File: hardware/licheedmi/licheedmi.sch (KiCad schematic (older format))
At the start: 64 parts, among them J1 Conn_01x09, J2 HDMI_A_PCB, J3 LicheePiNano_LCD, J4 HDMI_A, U1 TDA19988, U2 LicheeNano, U3 TS3DV20812, U4 SC6206B

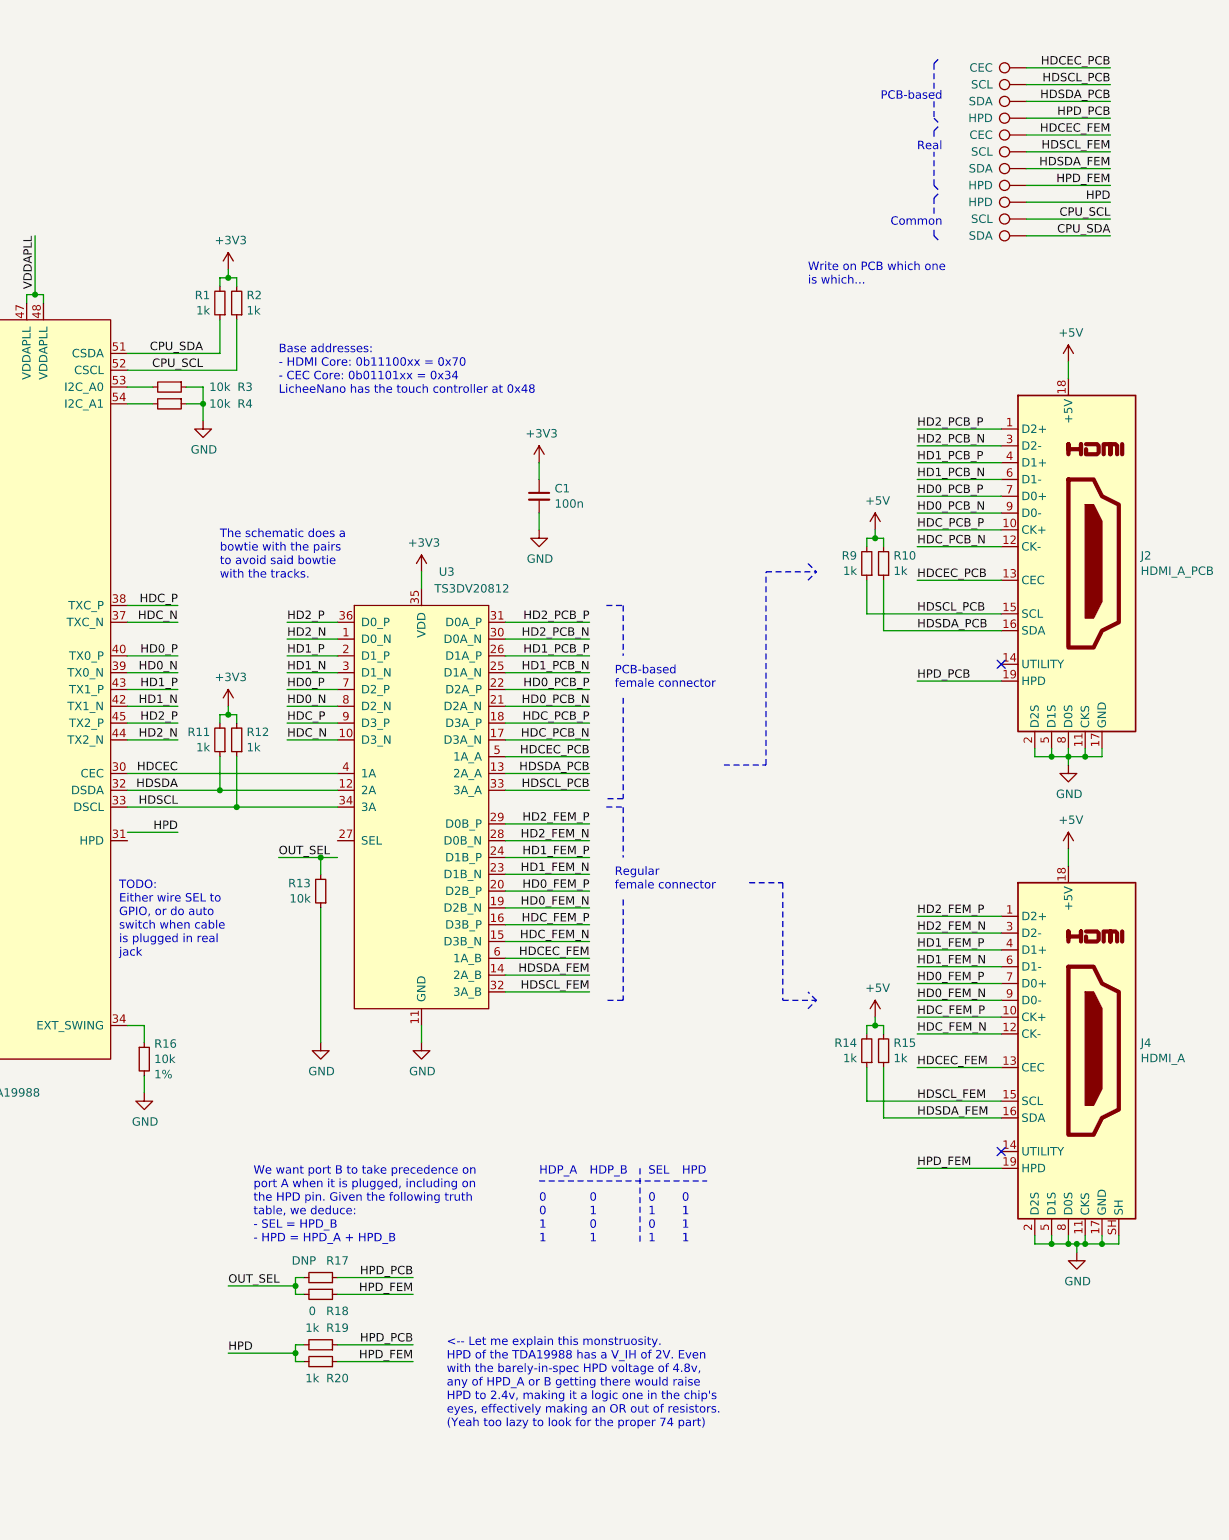
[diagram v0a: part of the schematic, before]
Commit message: sch: Draw wires rather than labels where wiring is straightforward
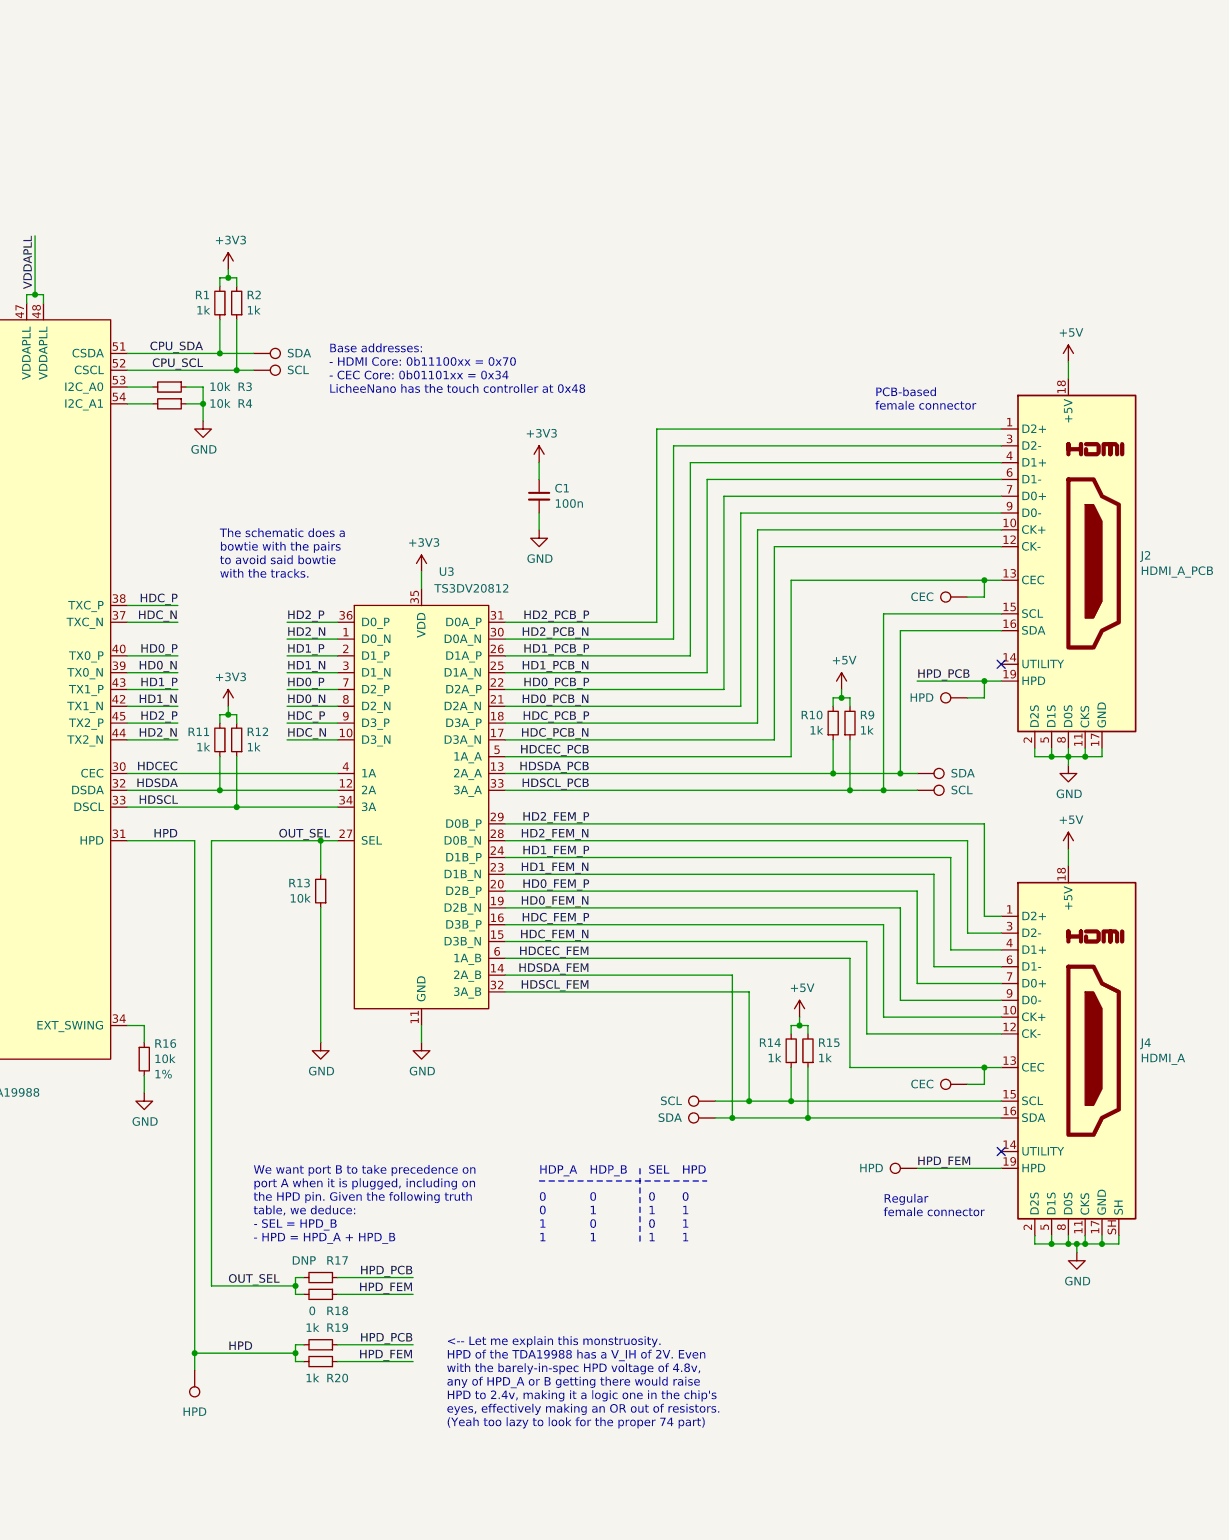
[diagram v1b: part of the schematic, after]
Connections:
- net HPD: now also U1.31 (HPD)
- net OUT_SEL: now also U3.27 (SEL)
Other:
- note removed: "Common"
- note removed: "PCB-based"
- note removed: "Real"
- note removed: "TODO:\nEither wire SEL to\nGPIO, or do auto\nswitch when cable\nis plugged in real\njack"
- note removed: "Write on PCB which one\nis which..."
- moved on the sheet: R10, R14, R15, R9

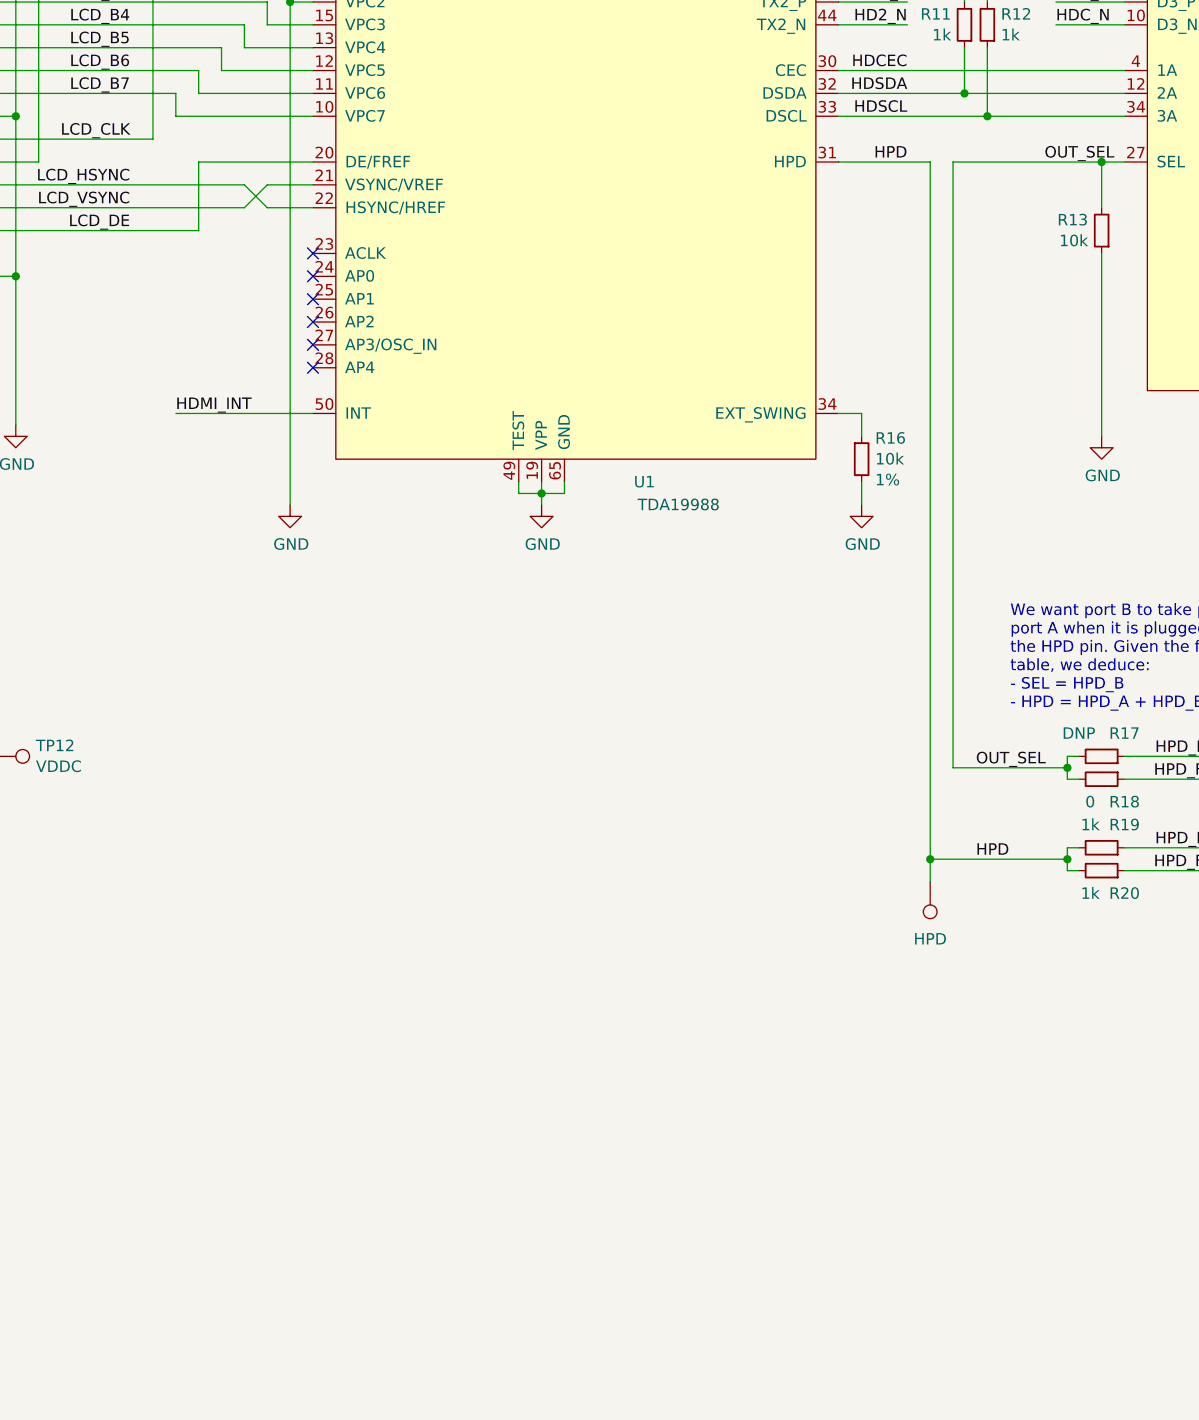
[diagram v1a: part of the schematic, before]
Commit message: *: Add USB-UART chip (CH340C)
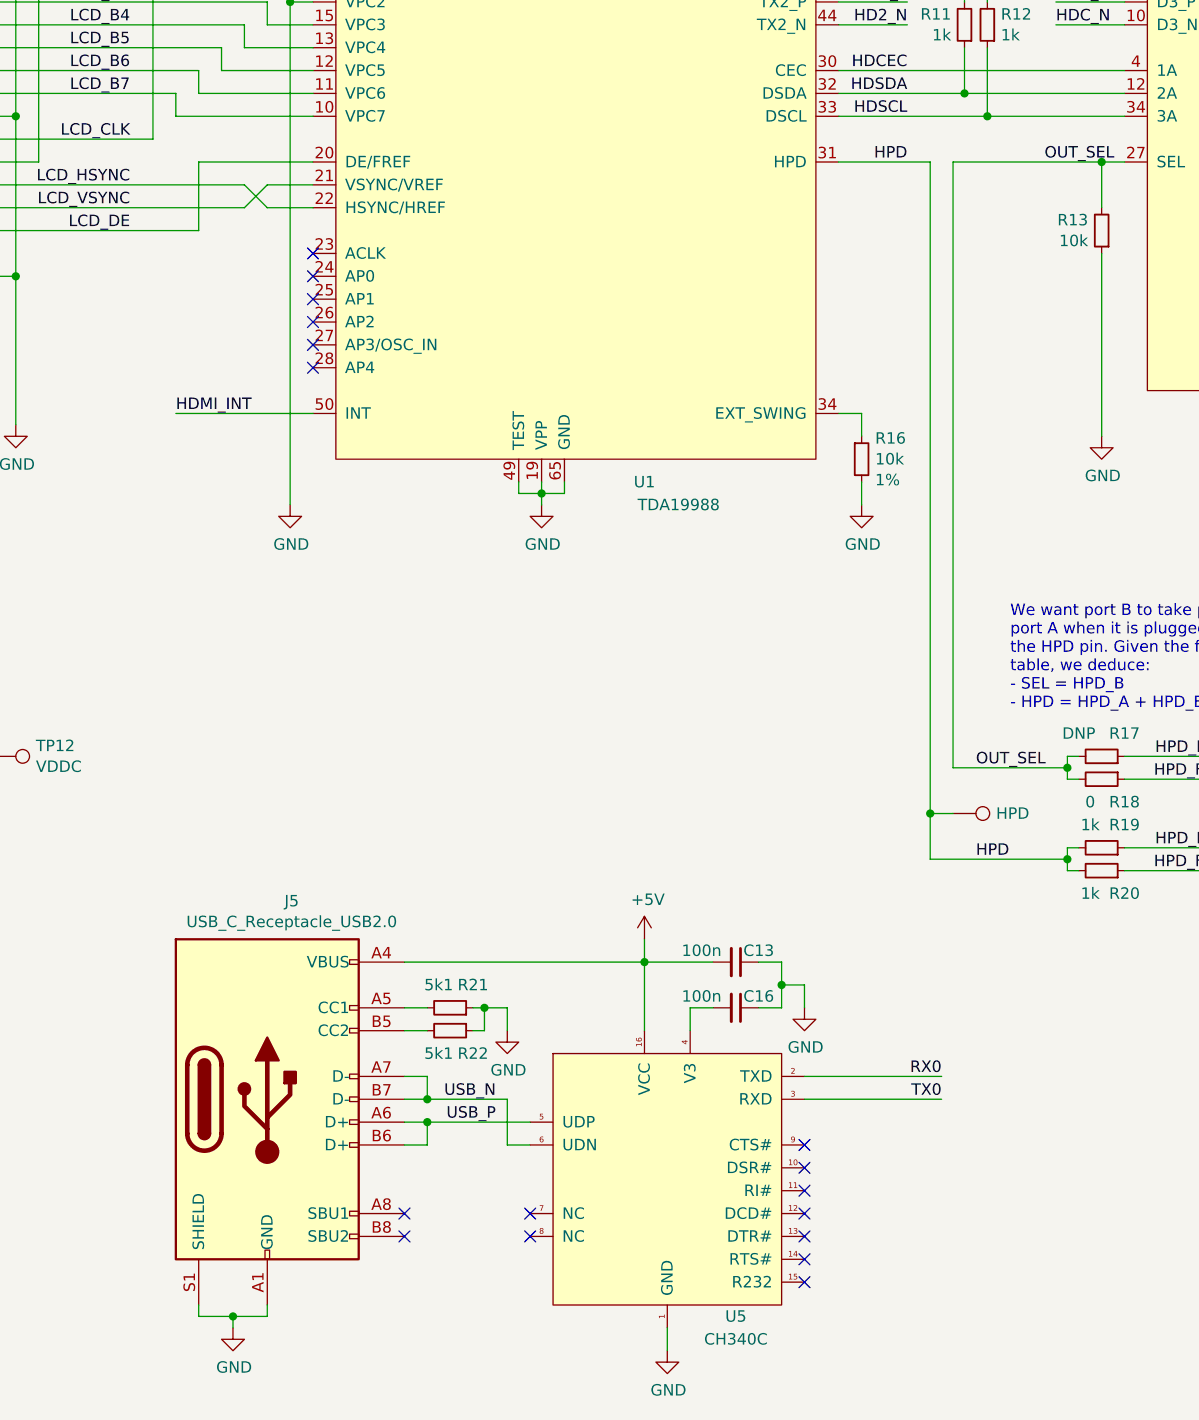
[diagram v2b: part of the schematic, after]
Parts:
- added C13, C16: 100n, Capacitor_SMD:C_0603_1608Metric, symbol Device:C_Small
- added J5: USB_C_Receptacle_USB2.0, hdmizness:USB_C_Receptacle_Palconn_UTC16-G, symbol Connector:USB_C_Receptacle_USB2.0
- added R21, R22: 5k1, Resistor_SMD:R_0603_1608Metric, symbol Device:R_Small
- added U5: CH340C, Package_SO:SOIC-16_3.9x9.9mm_P1.27mm, symbol hdmizness:CH340C
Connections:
- net +5V: now also C13.2, J5.A4 (VBUS), J5.A9 (VBUS), J5.B4 (VBUS), J5.B9 (VBUS), U5.16 (VCC)
- net GND: now also C13.1, C16.1, J5.A1 (GND), J5.A12 (GND), J5.B1 (GND), J5.B12 (GND), J5.S1 (SHIELD), R21.1, R22.1, U5.1 (GND)
- net RX0: now also U5.2 (TXD)
- net TX0: now also U5.3 (RXD)
- new net: J5.A5 (CC1), R21.2
- new net: J5.B5 (CC2), R22.2
- new net: C16.2, U5.4 (V3)
- new net USB_N: J5.A7 (D-), J5.B7 (D-), U5.6 (UDN)
- new net USB_P: J5.A6 (D+), J5.B6 (D+), U5.5 (UDP)
- no-connect marks 42 -> 53
